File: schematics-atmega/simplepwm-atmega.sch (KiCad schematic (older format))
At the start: 25 parts, among them J1 DEBUG: UART TxD, J2 DEBUG: Main loop indicator, J3 AVR-ISP-6, J4 PWM_OUTPUT, J5 PWM_OUTPUT, J6 PWM_OUTPUT, J7 Conn_01x01_Male, J8 Conn_01x01_Male, J9 Conn_01x01_Male, Q1 Q_NMOS, Q2 Q_NMOS, Q3 Q_NMOS, U1 ATmega

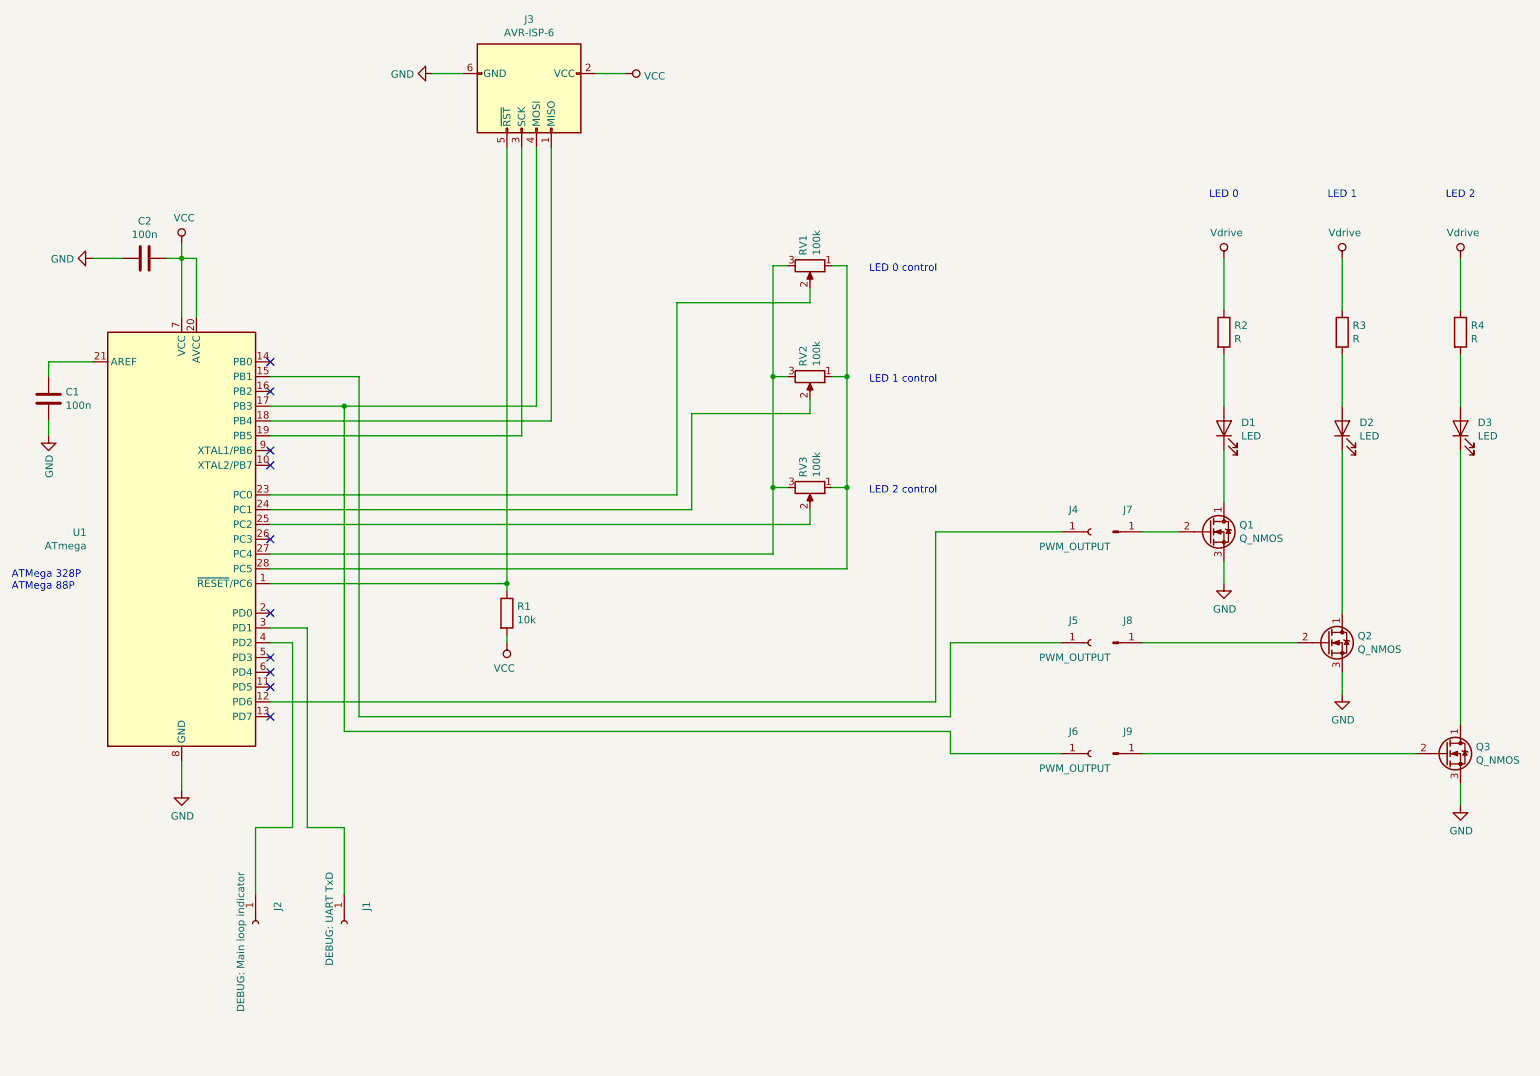
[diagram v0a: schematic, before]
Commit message: schematics: Add pull down at output stages
Signed-off-by: Michael Buesch <m@bues.ch>
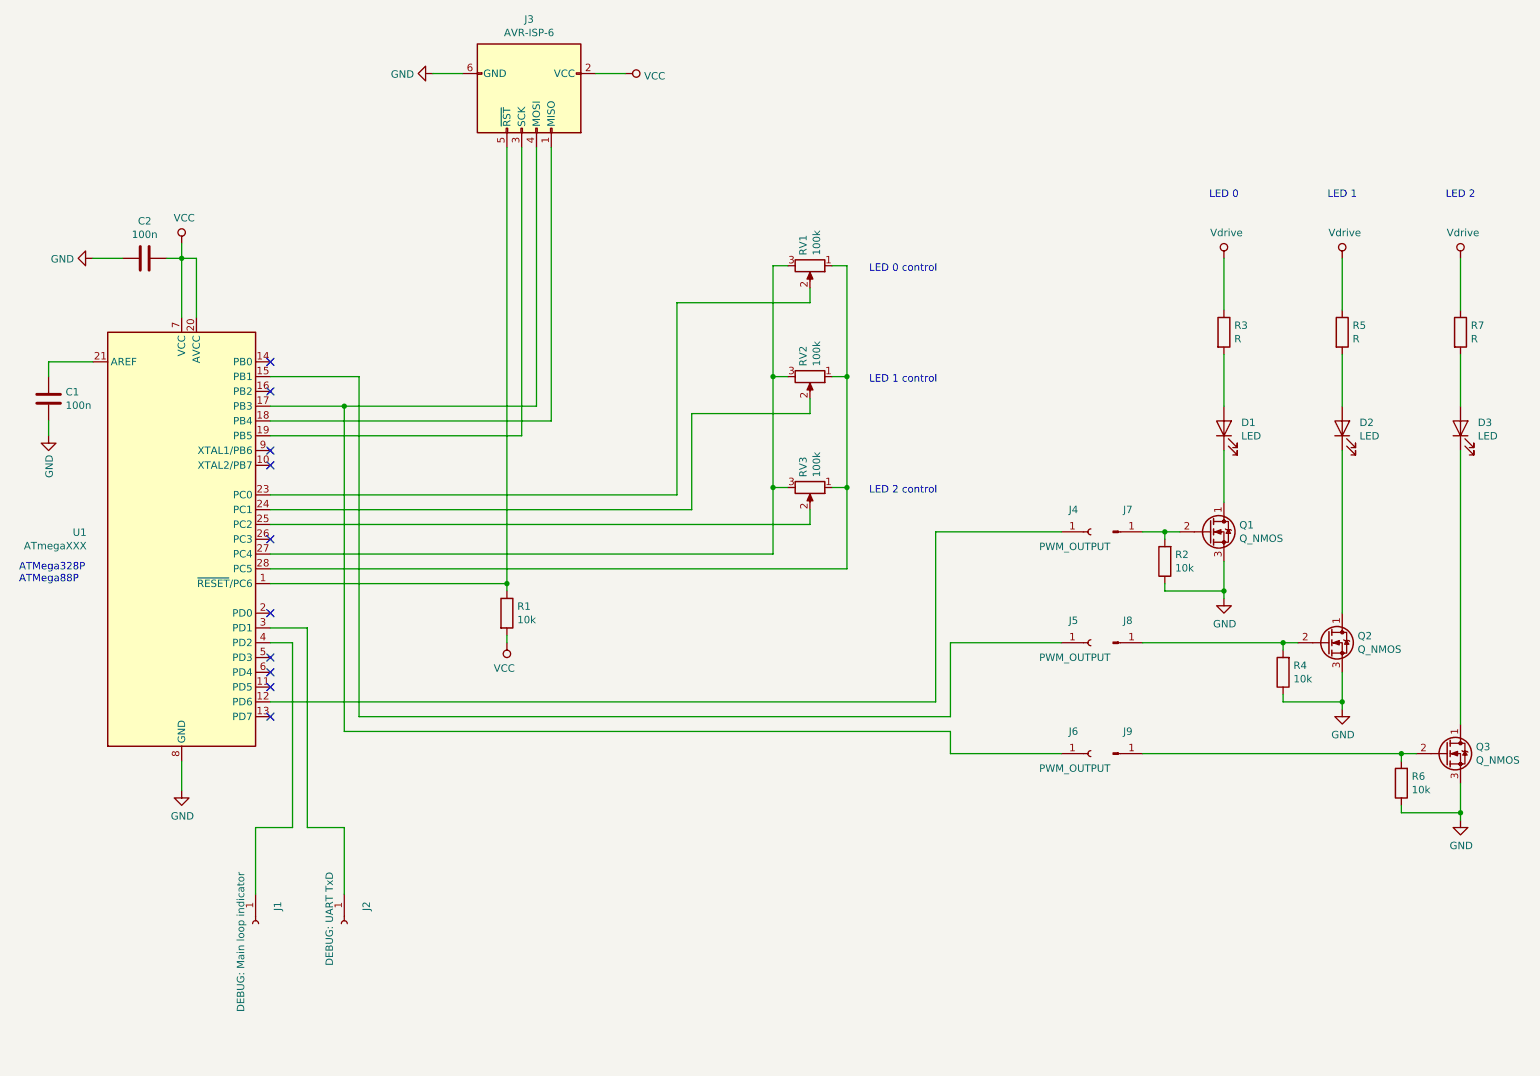
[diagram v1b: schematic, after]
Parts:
- added R2, R4, R6: 10k, symbol Device:R
- U1: value ATmega -> ATmegaXXX
- renumbered J2 to J1, J1 to J2, R2 to R3, R3 to R5, R4 to R7
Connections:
- net GND: now also R2.1, R4.1, R6.1
- net at J7.1 (Pin_1), Q1.2 (G): now also R2.2
- net at J8.1 (Pin_1), Q2.2 (G): now also R4.2
- net at J9.1 (Pin_1), Q3.2 (G): now also R6.2
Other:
- note added: "ATMega328P\nATMega88P"
- note removed: "ATMega 328P\nATMega 88P"
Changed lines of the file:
@@
 $EndComp
 $Comp
-L power:GND #PWR06
+L power:GND #PWR05
 U 1 1 5E1565B8
 P 3600 1050
-F 0 "#PWR06" H 3600 800 50  0001 C CNN
+F 0 "#PWR05" H 3600 800 50  0001 C CNN
 F 1 "GND" V 3605 922 50  0000 R CNN
 F 2 "" H 3600 1050 50  0001 C CNN
@@
 	4400 3400 2500 3400
 $Comp
-L power:VCC #PWR05
+L power:VCC #PWR06
 U 1 1 5E159838
 P 4100 4900
-F 0 "#PWR05" H 4100 4750 50  0001 C CNN
+F 0 "#PWR06" H 4100 4750 50  0001 C CNN
 F 1 "VCC" H 4118 5073 50  0000 C CNN
 F 2 "" H 4100 4900 50  0001 C CNN
@@
 $EndComp
 $Comp
-L Device:R R2
+L Device:R R3
 U 1 1 5E17B11C
 P 8950 2800
-F 0 "R2" H 9020 2846 50  0000 L CNN
+F 0 "R3" H 9020 2846 50  0000 L CNN
 F 1 "R" H 9020 2755 50  0000 L CNN
 F 2 "" V 8880 2800 50  0001 C CNN
@@
 L power:GND #PWR09
 U 1 1 5E17C420
-P 8950 4500
-F 0 "#PWR09" H 8950 4250 50  0001 C CNN
-F 1 "GND" H 8955 4327 50  0000 C CNN
-F 2 "" H 8950 4500 50  0001 C CNN
-F 3 "" H 8950 4500 50  0001 C CNN
-	1    8950 4500
-	1    0    0    -1
-$EndComp
-Wire Wire Line
-	8950 4350 8950 4500
-Wire Wire Line
-	8400 4150 8650 4150
+P 8950 4600
+F 0 "#PWR09" H 8950 4350 50  0001 C CNN
+F 1 "GND" H 8955 4427 50  0000 C CNN
+F 2 "" H 8950 4600 50  0001 C CNN
+F 3 "" H 8950 4600 50  0001 C CNN
+	1    8950 4600
+	1    0    0    -1
+$EndComp
+Wire Wire Line
+	8950 4350 8950 4550
+Wire Wire Line
+	8400 4150 8550 4150
 Wire Wire Line
 	8950 3600 8950 3950
@@
 P 1900 4200
 F 0 "U1" H 1257 4246 50  0000 R CNN
-F 1 "ATmega" H 1257 4155 50  0000 R CNN
+F 1 "ATmegaXXX" H 1257 4155 50  0000 R CNN
 F 2 "Package_DIP:DIP-28_W7.62mm" H 1900 4200 50  0001 C CIN
 F 3 "http://ww1.microchip.com/downloads/en/DeviceDoc/ATmega328_P%20AVR%20MCU%20with%20picoPower%20Technology%20Data%20Sheet%2040001984A.pdf" H 1900 4200 50  0001 C CNN
@@
 	1    0    0    -1
 $EndComp
-Text Notes 750  4550 0    50   ~ 0
-ATMega 328P\nATMega 88P
+Text Notes 800  4500 0    50   ~ 0
+ATMega328P\nATMega88P
 Wire Wire Line
 	1900 2300 2000 2300
@@
 $EndComp
 $Comp
-L Device:R R3
+L Device:R R5
 U 1 1 5E94F5AF
 P 9750 2800
-F 0 "R3" H 9820 2846 50  0000 L CNN
+F 0 "R5" H 9820 2846 50  0000 L CNN
 F 1 "R" H 9820 2755 50  0000 L CNN
 F 2 "" V 9680 2800 50  0001 C CNN
@@
 L power:GND #PWR011
 U 1 1 5E94F5BB
-P 9750 5250
-F 0 "#PWR011" H 9750 5000 50  0001 C CNN
-F 1 "GND" H 9755 5077 50  0000 C CNN
-F 2 "" H 9750 5250 50  0001 C CNN
-F 3 "" H 9750 5250 50  0001 C CNN
-	1    9750 5250
-	1    0    0    -1
-$EndComp
-Wire Wire Line
-	9750 5100 9750 5250
-Wire Wire Line
-	8400 4900 9450 4900
+P 9750 5350
+F 0 "#PWR011" H 9750 5100 50  0001 C CNN
+F 1 "GND" H 9755 5177 50  0000 C CNN
+F 2 "" H 9750 5350 50  0001 C CNN
+F 3 "" H 9750 5350 50  0001 C CNN
+	1    9750 5350
+	1    0    0    -1
+$EndComp
+Wire Wire Line
+	9750 5100 9750 5300
+Wire Wire Line
+	8400 4900 9350 4900
 Wire Wire Line
 	9750 3600 9750 4700
@@
 $EndComp
 $Comp
-L Device:R R4
+L Device:R R7
 U 1 1 5E951D3E
 P 10550 2800
-F 0 "R4" H 10620 2846 50  0000 L CNN
+F 0 "R7" H 10620 2846 50  0000 L CNN
 F 1 "R" H 10620 2755 50  0000 L CNN
 F 2 "" V 10480 2800 50  0001 C CNN
@@
 L power:GND #PWR013
 U 1 1 5E951D4A
-P 10550 6000
-F 0 "#PWR013" H 10550 5750 50  0001 C CNN
-F 1 "GND" H 10555 5827 50  0000 C CNN
-F 2 "" H 10550 6000 50  0001 C CNN
-F 3 "" H 10550 6000 50  0001 C CNN
-	1    10550 6000
-	1    0    0    -1
-$EndComp
-Wire Wire Line
-	10550 5850 10550 6000
-Wire Wire Line
-	8400 5650 10250 5650
+P 10550 6100
+F 0 "#PWR013" H 10550 5850 50  0001 C CNN
+F 1 "GND" H 10555 5927 50  0000 C CNN
+F 2 "" H 10550 6100 50  0001 C CNN
+F 3 "" H 10550 6100 50  0001 C CNN
+	1    10550 6100
+	1    0    0    -1
+$EndComp
+Wire Wire Line
+	10550 5850 10550 6050
+Wire Wire Line
+	8400 5650 10150 5650
 Wire Wire Line
 	10550 2950 10550 3300
@@
 NoConn ~ 2500 3600
 $Comp
-L Connector:Conn_01x01_Female J2
+L Connector:Conn_01x01_Female J1
 U 1 1 5EAD3DBC
 P 2400 6800
-F 0 "J2" H 2250 6950 50  0000 L CNN
+F 0 "J1" H 2250 6950 50  0000 L CNN
 F 1 "DEBUG: Main loop indicator" H 2050 6700 50  0000 L CNN
 F 2 "" H 2400 6800 50  0001 C CNN
@@
 	2400 6150 2400 6600
 $Comp
-L Connector:Conn_01x01_Female J1
+L Connector:Conn_01x01_Female J2
 U 1 1 5EB0AFE8
 P 3000 6800
-F 0 "J1" H 2850 6950 50  0000 L CNN
+F 0 "J2" H 2850 6950 50  0000 L CNN
 F 1 "DEBUG: UART TxD" H 2650 6700 50  0000 L CNN
 F 2 "" H 3000 6800 50  0001 C CNN
@@
 Wire Wire Line
 	2750 6150 3000 6150
+$Comp
+L Device:R R2
+U 1 1 5E91D052
+P 8550 4350
+F 0 "R2" H 8480 4304 50  0000 R CNN
+F 1 "10k" H 8480 4395 50  0000 R CNN
+F 2 "" V 8480 4350 50  0001 C CNN
+F 3 "~" H 8550 4350 50  0001 C CNN
+	1    8550 4350
+	-1   0    0    1
+$EndComp
+Wire Wire Line
+	8550 4200 8550 4150
+Connection ~ 8550 4150
+Wire Wire Line
+	8550 4150 8650 4150
+Wire Wire Line
+	8550 4500 8550 4550
+Wire Wire Line
+	8550 4550 8950 4550
+Connection ~ 8950 4550
+Wire Wire Line
+	8950 4550 8950 4600
+$Comp
+L Device:R R4
+U 1 1 5E92E1E4
+P 9350 5100
+F 0 "R4" H 9280 5054 50  0000 R CNN
+F 1 "10k" H 9280 5145 50  0000 R CNN
+F 2 "" V 9280 5100 50  0001 C CNN
+F 3 "~" H 9350 5100 50  0001 C CNN
+	1    9350 5100
+	-1   0    0    1
+$EndComp
+$Comp
+L Device:R R6
+U 1 1 5E92F1DD
+P 10150 5850
+F 0 "R6" H 10080 5804 50  0000 R CNN
+F 1 "10k" H 10080 5895 50  0000 R CNN
+F 2 "" V 10080 5850 50  0001 C CNN
+F 3 "~" H 10150 5850 50  0001 C CNN
+	1    10150 5850
+	-1   0    0    1
+$EndComp
+Wire Wire Line
+	9350 4950 9350 4900
+Connection ~ 9350 4900
+Wire Wire Line
+	9350 4900 9450 4900
+Wire Wire Line
+	9350 5250 9350 5300
+Wire Wire Line
+	9350 5300 9750 5300
+Connection ~ 9750 5300
+Wire Wire Line
+	9750 5300 9750 5350
+Wire Wire Line
+	10150 5700 10150 5650
+Connection ~ 10150 5650
+Wire Wire Line
+	10150 5650 10250 5650
+Wire Wire Line
+	10150 6000 10150 6050
+Wire Wire Line
+	10150 6050 10550 6050
+Connection ~ 10550 6050
+Wire Wire Line
+	10550 6050 10550 6100
 $EndSCHEMATC

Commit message: Minor updates to documentation
Signed-off-by: Michael Buesch <m@bues.ch>
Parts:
- added J3: UART RxD, symbol Connector:Conn_01x01_Female
- J2: value DEBUG: UART TxD -> UART TxD
- renumbered J9 to J10, J3 to J4, J4 to J5, J5 to J6, J6 to J7, J7 to J8, J8 to J9
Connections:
- net at U1.2 (PD0): now also J3.1 (Pin_1)
- no-connect marks 10 -> 9
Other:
- note added: "ATMega328P"
- note removed: "ATMega328P\nATMega88P"
- moved on the sheet: J1, J2
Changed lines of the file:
@@
 $EndDescr
 $Comp
-L Connector:AVR-ISP-6 J3
+L Connector:AVR-ISP-6 J4
 U 1 1 5E14DD07
 P 4200 1150
-F 0 "J3" V 3733 1200 50  0000 C CNN
+F 0 "J4" V 3733 1200 50  0000 C CNN
 F 1 "AVR-ISP-6" V 3824 1200 50  0000 C CNN
 F 2 "" V 3950 1200 50  0001 C CNN
@@
 	4100 4850 4100 4900
 $Comp
-L Connector:Conn_01x01_Female J4
+L Connector:Conn_01x01_Female J5
 U 1 1 5E15A9D4
 P 8050 4150
-F 0 "J4" H 7900 4300 50  0000 L CNN
+F 0 "J5" H 7900 4300 50  0000 L CNN
 F 1 "PWM_OUTPUT" H 7700 4050 50  0000 L CNN
 F 2 "" H 8050 4150 50  0001 C CNN
@@
 $EndComp
 $Comp
-L Connector:Conn_01x01_Male J7
+L Connector:Conn_01x01_Male J8
 U 1 1 5E177271
 P 8200 4150
-F 0 "J7" H 8300 4300 50  0000 C CNN
+F 0 "J8" H 8300 4300 50  0000 C CNN
 F 1 "Conn_01x01_Male" H 8200 4050 50  0001 C CNN
 F 2 "" H 8200 4150 50  0001 C CNN
@@
 $EndComp
 Text Notes 800  4500 0    50   ~ 0
-ATMega328P\nATMega88P
+ATMega328P
 Wire Wire Line
 	1900 2300 2000 2300
@@
 	4300 3300 3000 3300
 $Comp
-L Connector:Conn_01x01_Male J8
+L Connector:Conn_01x01_Male J9
 U 1 1 5E94F59D
 P 8200 4900
-F 0 "J8" H 8300 5050 50  0000 C CNN
+F 0 "J9" H 8300 5050 50  0000 C CNN
 F 1 "Conn_01x01_Male" H 8200 4800 50  0001 C CNN
 F 2 "" H 8200 4900 50  0001 C CNN
@@
 	9750 2300 9750 2650
 $Comp
-L Connector:Conn_01x01_Male J9
+L Connector:Conn_01x01_Male J10
 U 1 1 5E951D2C
 P 8200 5650
-F 0 "J9" H 8300 5800 50  0000 C CNN
+F 0 "J10" H 8300 5800 50  0000 C CNN
 F 1 "Conn_01x01_Male" H 8200 5550 50  0001 C CNN
 F 2 "" H 8200 5650 50  0001 C CNN
@@
 	10550 3600 10550 5450
 $Comp
-L Connector:Conn_01x01_Female J5
+L Connector:Conn_01x01_Female J6
 U 1 1 5E97EE1E
 P 8050 4900
-F 0 "J5" H 7900 5050 50  0000 L CNN
+F 0 "J6" H 7900 5050 50  0000 L CNN
 F 1 "PWM_OUTPUT" H 7700 4800 50  0000 L CNN
 F 2 "" H 8050 4900 50  0001 C CNN
@@
 $EndComp
 $Comp
-L Connector:Conn_01x01_Female J6
+L Connector:Conn_01x01_Female J7
 U 1 1 5E980565
 P 8050 5650
-F 0 "J6" H 7900 5800 50  0000 L CNN
+F 0 "J7" H 7900 5800 50  0000 L CNN
 F 1 "PWM_OUTPUT" H 7700 5550 50  0000 L CNN
 F 2 "" H 8050 5650 50  0001 C CNN
@@
 L Connector:Conn_01x01_Female J1
 U 1 1 5EAD3DBC
-P 2400 6800
-F 0 "J1" H 2250 6950 50  0000 L CNN
-F 1 "DEBUG: Main loop indicator" H 2050 6700 50  0000 L CNN
-F 2 "" H 2400 6800 50  0001 C CNN
-F 3 "~" H 2400 6800 50  0001 C CNN
-	1    2400 6800
-	0    1    1    0
-$EndComp
-NoConn ~ 2500 4700
+P 2100 6800
+F 0 "J1" H 1950 6950 50  0000 L CNN
+F 1 "DEBUG: Main loop indicator" H 1750 6700 50  0000 L CNN
+F 2 "" H 2100 6800 50  0001 C CNN
+F 3 "~" H 2100 6800 50  0001 C CNN
+	1    2100 6800
+	0    1    1    0
+$EndComp
 NoConn ~ 2500 5000
 NoConn ~ 2500 5100
@@
 	2500 4900 2650 4900
 Wire Wire Line
-	2400 6150 2400 6600
+	2100 6150 2100 6600
 $Comp
 L Connector:Conn_01x01_Female J2
 U 1 1 5EB0AFE8
-P 3000 6800
-F 0 "J2" H 2850 6950 50  0000 L CNN
-F 1 "DEBUG: UART TxD" H 2650 6700 50  0000 L CNN
-F 2 "" H 3000 6800 50  0001 C CNN
-F 3 "~" H 3000 6800 50  0001 C CNN
-	1    3000 6800
+P 2750 6800
+F 0 "J2" H 2600 6950 50  0000 L CNN
+F 1 "UART TxD" H 2400 6700 50  0000 L CNN
+F 2 "" H 2750 6800 50  0001 C CNN
+F 3 "~" H 2750 6800 50  0001 C CNN
+	1    2750 6800
 	0    1    1    0
 $EndComp
@@
 Connection ~ 4100 4500
 Wire Wire Line
-	2650 6150 2400 6150
+	2650 6150 2100 6150
 Wire Wire Line
 	2650 4900 2650 6150
 NoConn ~ 2500 3700
-Wire Wire Line
-	2750 4800 2750 6150
-Wire Wire Line
-	3000 6150 3000 6600
-Wire Wire Line
-	2750 6150 3000 6150
 $Comp
 L Device:R R2
@@
 Wire Wire Line
 	10550 6050 10550 6100
+$Comp
+L Connector:Conn_01x01_Female J3
+U 1 1 5EB9E2A5
+P 3200 6800
+F 0 "J3" H 3050 6950 50  0000 L CNN
+F 1 "UART RxD" H 2850 6700 50  0000 L CNN
+F 2 "" H 3200 6800 50  0001 C CNN
+F 3 "~" H 3200 6800 50  0001 C CNN
+	1    3200 6800
+	0    1    1    0
+$EndComp
+Wire Wire Line
+	2500 4700 2850 4700
+Wire Wire Line
+	2850 4700 2850 6150
+Wire Wire Line
+	2850 6150 3200 6150
+Wire Wire Line
+	3200 6150 3200 6600
+Wire Wire Line
+	2750 4800 2750 6600
 $EndSCHEMATC
